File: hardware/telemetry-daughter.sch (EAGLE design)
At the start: 17 parts, among them J1 GPS1, J2 MICRO-SD_CARD_SOCKET, J3 IO, J6 SMA_EDGE, U2 9DoF IMU

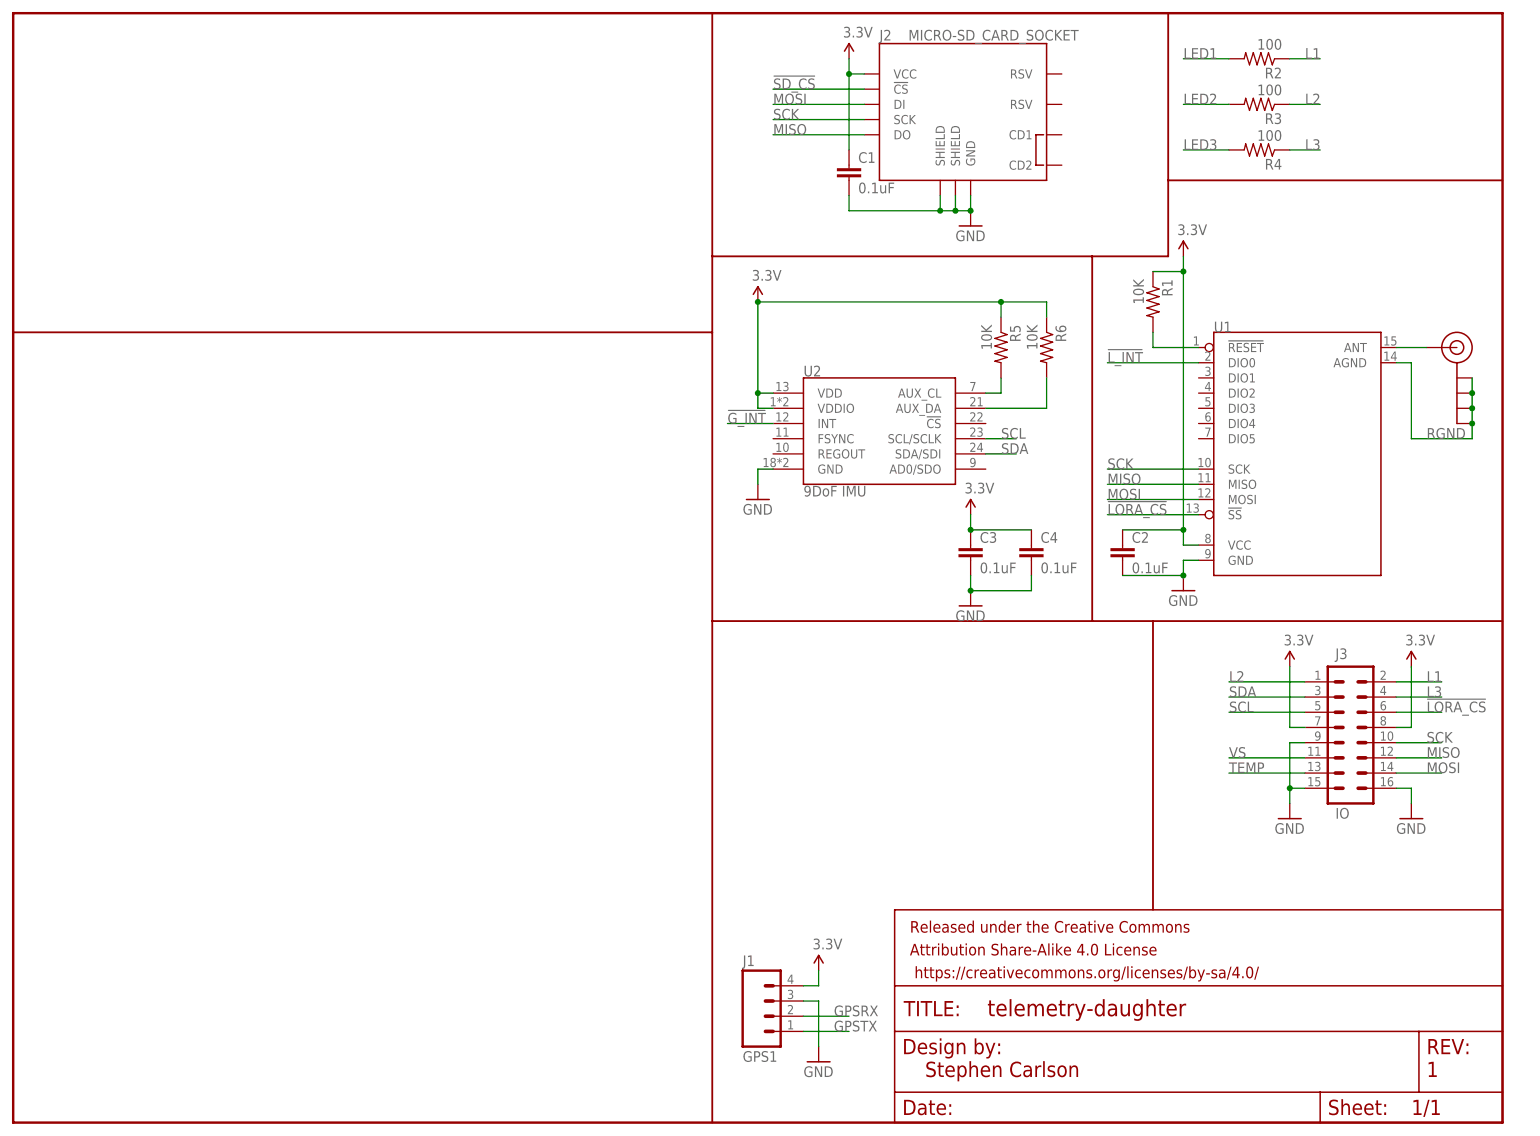
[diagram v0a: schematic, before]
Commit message: Update telemetry daughter board, a few nets left to route, need to check connector placement and sizing
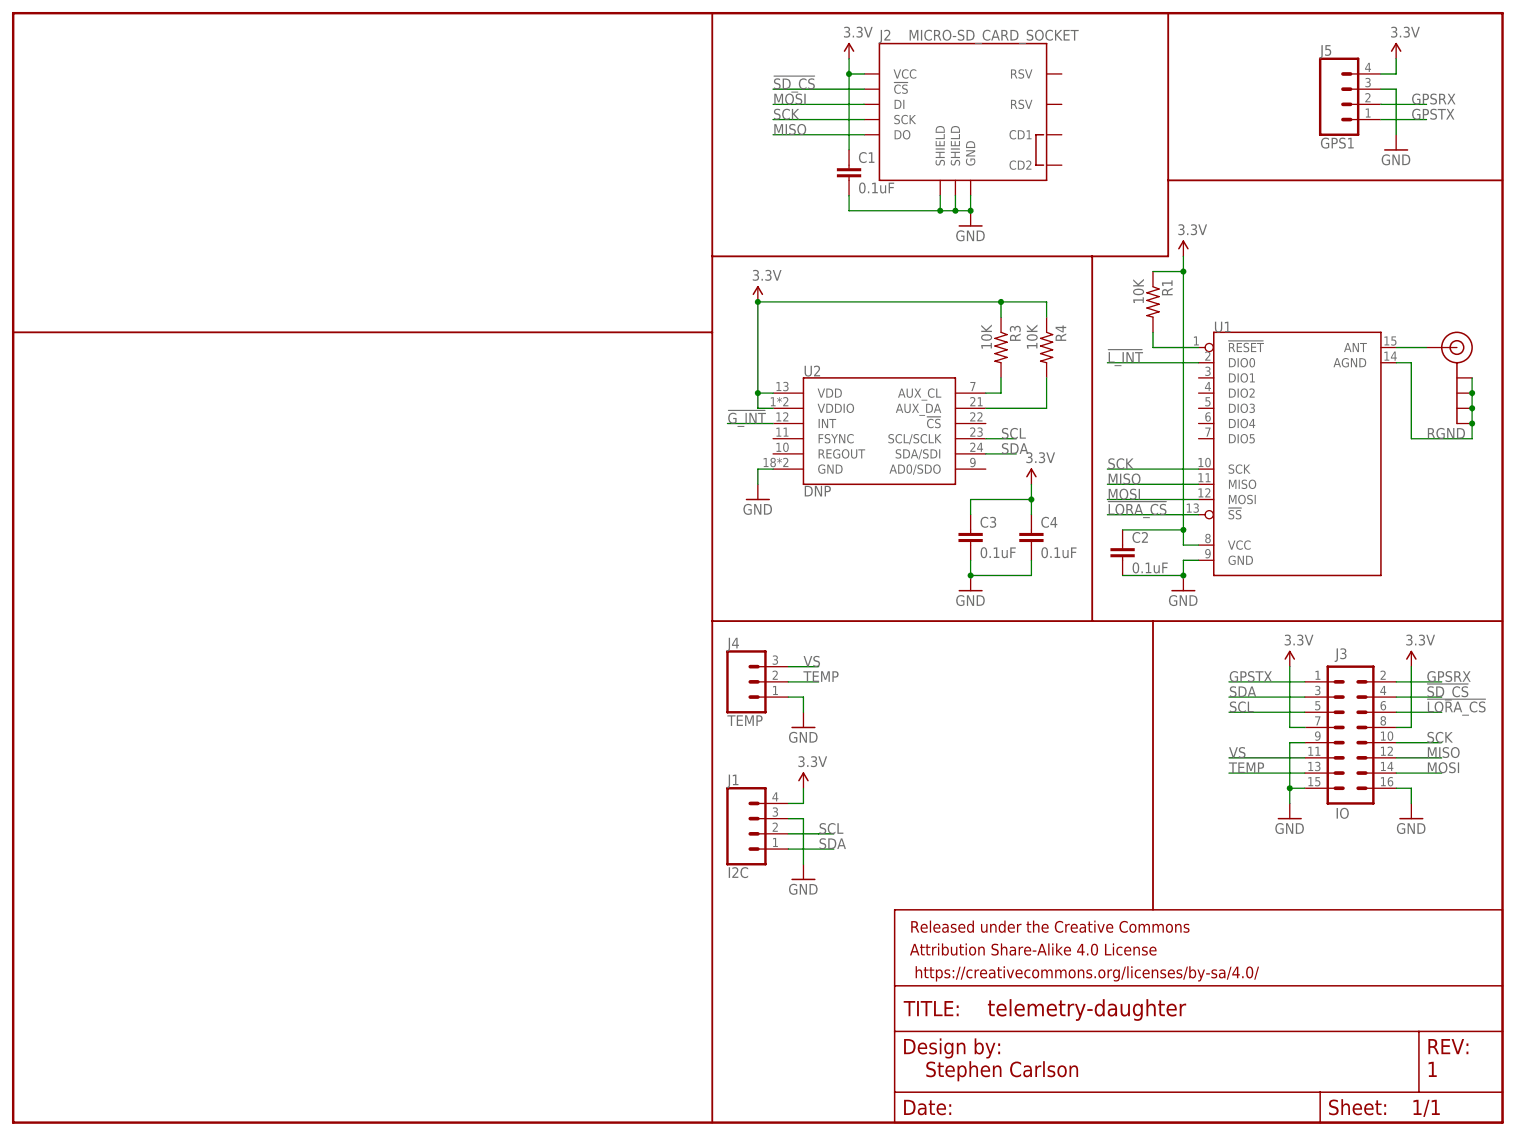
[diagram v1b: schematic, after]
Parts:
- removed R2: 100, SparkFun-Passives:RESISTOR0805-RES
- removed R5, R6: 10K, SparkFun-Passives:RESISTOR0805-RES
- added J4: TEMP, SparkFun-Connectors:CONN_03JST-PTH
- added J5: GPS1, SparkFun-Connectors:CONN_04JST-PTH
- J1: value GPS1 -> I2C; device SparkFun-Connectors:M04PTH -> SparkFun-Connectors:CONN_04JST-PTH
- R3, R4: value 100 -> 10K
- U2: value 9DoF IMU -> DNP
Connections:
- removed net L1: J3.2, R2.1
- removed net L2: J3.1, R3.1
- removed net L3: J3.4, R4.1
- removed net LED1: R2.2
- removed net LED2: R3.2
- removed net LED3: R4.2
- net !SD_CS!: now also J3.4
- net 3.3V: now also J5.4, R3.1, R4.1; no longer R5.1, R6.1
- net AUX_CL: now also R3.2; no longer R5.2
- net AUX_DA: now also R4.2; no longer R6.2
- net GND: now also J4.1, J5.3
- net GPSRX: now also J3.2, J5.2; no longer J1.2
- net GPSTX: now also J3.1, J5.1; no longer J1.1
- net SCL: now also J1.2
- net SDA: now also J1.1
- net TEMP: now also J4.2
- net VS: now also J4.3
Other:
- moved on the sheet: C3, C4, J1, R3, R4

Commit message: Connect CS and AD0 pins on the MPU9250. Fix a few small routing issues near the connector.
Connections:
- net GND: now also U2.!CS, U2.AD0/SDO
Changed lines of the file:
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@@
 <part name="SUPPLY5" library="SparkFun-Aesthetics" deviceset="3.3V" device=""/>
 <part name="GND8" library="SparkFun-Aesthetics" deviceset="GND" device=""/>
+<part name="GND7" library="SparkFun-Aesthetics" deviceset="GND" device=""/>
 </parts>
 <sheets>
@@
 <instance part="SUPPLY5" gate="G$1" x="132.08" y="55.88"/>
 <instance part="GND8" gate="1" x="132.08" y="40.64"/>
+<instance part="GND7" gate="1" x="177.8" y="104.14"/>
 </instances>
 <busses>
@@
 <wire x1="132.08" y1="50.8" x2="132.08" y2="43.18" width="0.1524" layer="91"/>
 </segment>
+<segment>
+<pinref part="U2" gate="G$1" pin="!CS"/>
+<wire x1="162.56" y1="116.84" x2="177.8" y2="116.84" width="0.1524" layer="91"/>
+<wire x1="177.8" y1="116.84" x2="177.8" y2="109.22" width="0.1524" layer="91"/>
+<pinref part="U2" gate="G$1" pin="AD0/SDO"/>
+<wire x1="177.8" y1="109.22" x2="162.56" y2="109.22" width="0.1524" layer="91"/>
+<pinref part="GND7" gate="1" pin="GND"/>
+<wire x1="177.8" y1="106.68" x2="177.8" y2="109.22" width="0.1524" layer="91"/>
+<junction x="177.8" y="109.22"/>
+</segment>
 </net>

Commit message: Change daughter card to use right angle SMA connector to remove conflict with enclosure
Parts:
- removed J6: SMA_EDGE, SparkFun-Connectors:SMA_EDGE
- added U$3: SMA_VERT, HAB:SMA_VERT
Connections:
- net RF_LORA: now also U$3.SIGNAL; no longer J6.SIGNAL
- net RGND: now also U$3.GND@0, U$3.GND@1, U$3.GND@2, U$3.GND@3; no longer J6.GND@0, J6.GND@1, J6.GND@2, J6.GND@3
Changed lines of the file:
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@@
 <parts>
 <part name="FRAME1" library="SparkFun-Aesthetics" deviceset="FRAME-LETTER" device="NO_PACKAGE"/>
-<part name="J6" library="SparkFun-Connectors" deviceset="SMA_EDGE" device=""/>
 <part name="GND42" library="SparkFun-Aesthetics" deviceset="GND" device=""/>
 <part name="SUPPLY16" library="SparkFun-Aesthetics" deviceset="3.3V" device=""/>
@@
 <part name="GND8" library="SparkFun-Aesthetics" deviceset="GND" device=""/>
 <part name="GND7" library="SparkFun-Aesthetics" deviceset="GND" device=""/>
+<part name="U$3" library="HAB" deviceset="SMA_VERT" device=""/>
 </parts>
 <sheets>
@@
 <instance part="FRAME1" gate="G$1" x="0" y="0"/>
 <instance part="FRAME1" gate="V" x="147.32" y="0"/>
-<instance part="J6" gate="1" x="241.3" y="129.54" rot="MR0"/>
 <instance part="GND42" gate="1" x="233.68" y="50.8"/>
 <instance part="SUPPLY16" gate="G$1" x="139.7" y="177.8"/>
@@
 <instance part="GND8" gate="1" x="132.08" y="40.64"/>
 <instance part="GND7" gate="1" x="177.8" y="104.14"/>
+<instance part="U$3" gate="G$1" x="241.3" y="129.54" rot="MR0"/>
 </instances>
 <busses>
@@
 <net name="RGND" class="0">
 <segment>
-<pinref part="J6" gate="1" pin="GND@3"/>
-<pinref part="J6" gate="1" pin="GND@2"/>
+<wire x1="243.84" y1="114.3" x2="243.84" y2="116.84" width="0.1524" layer="91"/>
 <wire x1="243.84" y1="116.84" x2="243.84" y2="119.38" width="0.1524" layer="91"/>
-<pinref part="J6" gate="1" pin="GND@1"/>
 <wire x1="243.84" y1="119.38" x2="243.84" y2="121.92" width="0.1524" layer="91"/>
-<junction x="243.84" y="119.38"/>
-<pinref part="J6" gate="1" pin="GND@0"/>
 <wire x1="243.84" y1="121.92" x2="243.84" y2="124.46" width="0.1524" layer="91"/>
-<junction x="243.84" y="121.92"/>
-<wire x1="243.84" y1="116.84" x2="243.84" y2="114.3" width="0.1524" layer="91"/>
-<junction x="243.84" y="116.84"/>
 <wire x1="243.84" y1="114.3" x2="233.68" y2="114.3" width="0.1524" layer="91"/>
 <wire x1="233.68" y1="114.3" x2="233.68" y2="127" width="0.1524" layer="91"/>
@@
 <wire x1="233.68" y1="127" x2="231.14" y2="127" width="0.1524" layer="91"/>
 <label x="236.22" y="114.3" size="1.778" layer="95"/>
+<pinref part="U$3" gate="G$1" pin="GND@0"/>
+<pinref part="U$3" gate="G$1" pin="GND@1"/>
+<junction x="243.84" y="121.92"/>
+<pinref part="U$3" gate="G$1" pin="GND@2"/>
+<junction x="243.84" y="119.38"/>
+<pinref part="U$3" gate="G$1" pin="GND@3"/>
+<junction x="243.84" y="116.84"/>
 </segment>
 </net>
@@
 <segment>
 <pinref part="U1" gate="G$1" pin="ANT"/>
-<pinref part="J6" gate="1" pin="SIGNAL"/>
 <wire x1="231.14" y1="129.54" x2="236.22" y2="129.54" width="0.1524" layer="91"/>
-</segment>
-</net>
+<pinref part="U$3" gate="G$1" pin="SIGNAL"/>
+</segment>
+</net>

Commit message: Change LoRA footprint on daughter card to the RA-02 which is easier to obtain
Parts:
- removed U$3: SMA_VERT, HAB:SMA_VERT
- U1: value (none) -> RA02; device HAB:DRF1278F -> HAB:RA02
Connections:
- removed net RF_LORA: U$3.SIGNAL, U1.ANT
- removed net RGND: U$3.GND@0, U$3.GND@1, U$3.GND@2, U$3.GND@3, U1.AGND
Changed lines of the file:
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@@
 <part name="SUPPLY10" library="SparkFun-Aesthetics" deviceset="3.3V" device=""/>
 <part name="SUPPLY23" library="SparkFun-Aesthetics" deviceset="3.3V" device=""/>
-<part name="U1" library="HAB" deviceset="DRF1278F" device=""/>
 <part name="J2" library="SparkFun-Connectors" deviceset="MICRO-SD_CARD_SOCKET" device=""/>
 <part name="GND1" library="SparkFun-Aesthetics" deviceset="GND" device=""/>
@@
 <part name="GND8" library="SparkFun-Aesthetics" deviceset="GND" device=""/>
 <part name="GND7" library="SparkFun-Aesthetics" deviceset="GND" device=""/>
-<part name="U$3" library="HAB" deviceset="SMA_VERT" device=""/>
+<part name="U1" library="HAB" deviceset="RA02" device=""/>
 </parts>
 <sheets>
@@
 <instance part="SUPPLY10" gate="G$1" x="233.68" y="76.2"/>
 <instance part="SUPPLY23" gate="G$1" x="213.36" y="76.2"/>
-<instance part="U1" gate="G$1" x="215.9" y="111.76"/>
 <instance part="J2" gate="1" x="157.48" y="170.18"/>
 <instance part="GND1" gate="1" x="160.02" y="149.86"/>
@@
 <instance part="GND8" gate="1" x="132.08" y="40.64"/>
 <instance part="GND7" gate="1" x="177.8" y="104.14"/>
-<instance part="U$3" gate="G$1" x="241.3" y="129.54" rot="MR0"/>
+<instance part="U1" gate="G$1" x="213.36" y="111.76"/>
 </instances>
 <busses>
@@
 <pinref part="GND2" gate="1" pin="GND"/>
 <wire x1="195.58" y1="91.44" x2="195.58" y2="93.98" width="0.1524" layer="91"/>
-<pinref part="U1" gate="G$1" pin="GND"/>
 <wire x1="195.58" y1="93.98" x2="198.12" y2="93.98" width="0.1524" layer="91"/>
 <pinref part="C2" gate="G$1" pin="2"/>
 <wire x1="185.42" y1="91.44" x2="195.58" y2="91.44" width="0.1524" layer="91"/>
 <junction x="195.58" y="91.44"/>
+<pinref part="U1" gate="G$1" pin="GND"/>
 </segment>
 <segment>
@@
 <pinref part="SUPPLY1" gate="G$1" pin="3.3V"/>
 <wire x1="195.58" y1="144.78" x2="195.58" y2="142.24" width="0.1524" layer="91"/>
-<pinref part="U1" gate="G$1" pin="VCC"/>
 <wire x1="195.58" y1="142.24" x2="195.58" y2="99.06" width="0.1524" layer="91"/>
 <wire x1="195.58" y1="99.06" x2="195.58" y2="96.52" width="0.1524" layer="91"/>
@@
 <wire x1="185.42" y1="99.06" x2="195.58" y2="99.06" width="0.1524" layer="91"/>
 <junction x="195.58" y="99.06"/>
+<pinref part="U1" gate="G$1" pin="VCC"/>
 </segment>
 <segment>
@@
 </segment>
 <segment>
-<pinref part="U1" gate="G$1" pin="MISO"/>
 <wire x1="182.88" y1="106.68" x2="198.12" y2="106.68" width="0.1524" layer="91"/>
 <label x="182.88" y="106.68" size="1.778" layer="95"/>
+<pinref part="U1" gate="G$1" pin="MISO"/>
 </segment>
 </net>
@@
 </segment>
 <segment>
-<pinref part="U1" gate="G$1" pin="MOSI"/>
 <wire x1="182.88" y1="104.14" x2="198.12" y2="104.14" width="0.1524" layer="91"/>
 <label x="182.88" y="104.14" size="1.778" layer="95"/>
+<pinref part="U1" gate="G$1" pin="MOSI"/>
 </segment>
 </net>
@@
 </segment>
 <segment>
-<pinref part="U1" gate="G$1" pin="SCK"/>
 <wire x1="182.88" y1="109.22" x2="198.12" y2="109.22" width="0.1524" layer="91"/>
 <label x="182.88" y="109.22" size="1.778" layer="95"/>
-</segment>
-</net>
-<net name="RGND" class="0">
-<segment>
-<wire x1="243.84" y1="114.3" x2="243.84" y2="116.84" width="0.1524" layer="91"/>
-<wire x1="243.84" y1="116.84" x2="243.84" y2="119.38" width="0.1524" layer="91"/>
-<wire x1="243.84" y1="119.38" x2="243.84" y2="121.92" width="0.1524" layer="91"/>
-<wire x1="243.84" y1="121.92" x2="243.84" y2="124.46" width="0.1524" layer="91"/>
-<wire x1="243.84" y1="114.3" x2="233.68" y2="114.3" width="0.1524" layer="91"/>
-<wire x1="233.68" y1="114.3" x2="233.68" y2="127" width="0.1524" layer="91"/>
-<pinref part="U1" gate="G$1" pin="AGND"/>
-<wire x1="233.68" y1="127" x2="231.14" y2="127" width="0.1524" layer="91"/>
-<label x="236.22" y="114.3" size="1.778" layer="95"/>
-<pinref part="U$3" gate="G$1" pin="GND@0"/>
-<pinref part="U$3" gate="G$1" pin="GND@1"/>
-<junction x="243.84" y="121.92"/>
-<pinref part="U$3" gate="G$1" pin="GND@2"/>
-<junction x="243.84" y="119.38"/>
-<pinref part="U$3" gate="G$1" pin="GND@3"/>
-<junction x="243.84" y="116.84"/>
+<pinref part="U1" gate="G$1" pin="SCK"/>
 </segment>
 </net>
@@
 </segment>
 </net>
-<net name="RF_LORA" class="0">
-<segment>
-<pinref part="U1" gate="G$1" pin="ANT"/>
-<wire x1="231.14" y1="129.54" x2="236.22" y2="129.54" width="0.1524" layer="91"/>
-<pinref part="U$3" gate="G$1" pin="SIGNAL"/>
-</segment>
-</net>
 <net name="!SD_CS!" class="0">
 <segment>
@@
 <net name="!LORA_CS!" class="0">
 <segment>
-<pinref part="U1" gate="G$1" pin="!SS!"/>
 <wire x1="182.88" y1="101.6" x2="198.12" y2="101.6" width="0.1524" layer="91"/>
 <label x="182.88" y="101.6" size="1.778" layer="95"/>
+<pinref part="U1" gate="G$1" pin="!SS!"/>
 </segment>
 <segment>
@@
 <net name="!L_INT!" class="0">
 <segment>
-<pinref part="U1" gate="G$1" pin="DIO0"/>
 <wire x1="182.88" y1="127" x2="198.12" y2="127" width="0.1524" layer="91"/>
 <label x="182.88" y="127" size="1.778" layer="95"/>
+<pinref part="U1" gate="G$1" pin="DIO0"/>
 </segment>
 </net>
 <net name="!LORA_RST!" class="0">
 <segment>
-<pinref part="U1" gate="G$1" pin="!RESET!"/>
 <pinref part="R1" gate="G$1" pin="2"/>
 <wire x1="198.12" y1="129.54" x2="190.5" y2="129.54" width="0.1524" layer="91"/>
 <wire x1="190.5" y1="129.54" x2="190.5" y2="132.08" width="0.1524" layer="91"/>
-</segment>
-</net>
+<pinref part="U1" gate="G$1" pin="!RESET!"/>
+</segment>
+</net>
